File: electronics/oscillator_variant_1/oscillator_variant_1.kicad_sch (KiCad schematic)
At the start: 48 parts, among them J1 module_2x15_left_input, J2 module_2x15_right_input, J3 Coax, Q1 BC817, U1 TL081, U2 LME49720, U3 TL082, U4 TL431

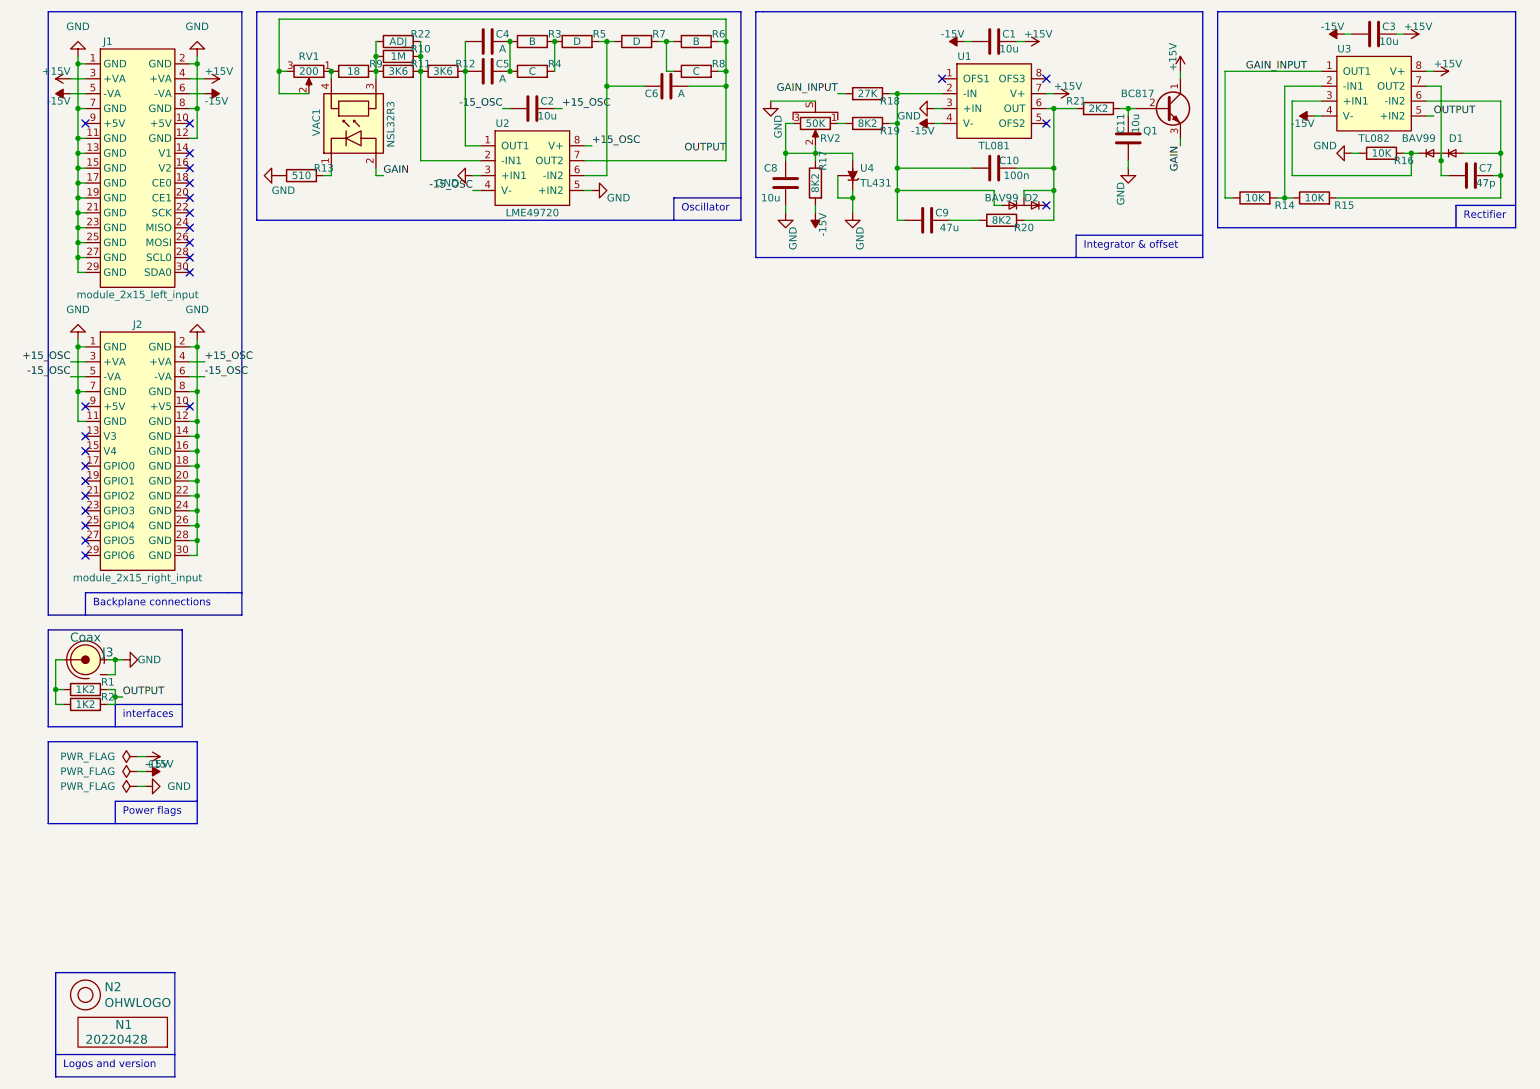
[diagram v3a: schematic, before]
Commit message: place and route and silk placement completed
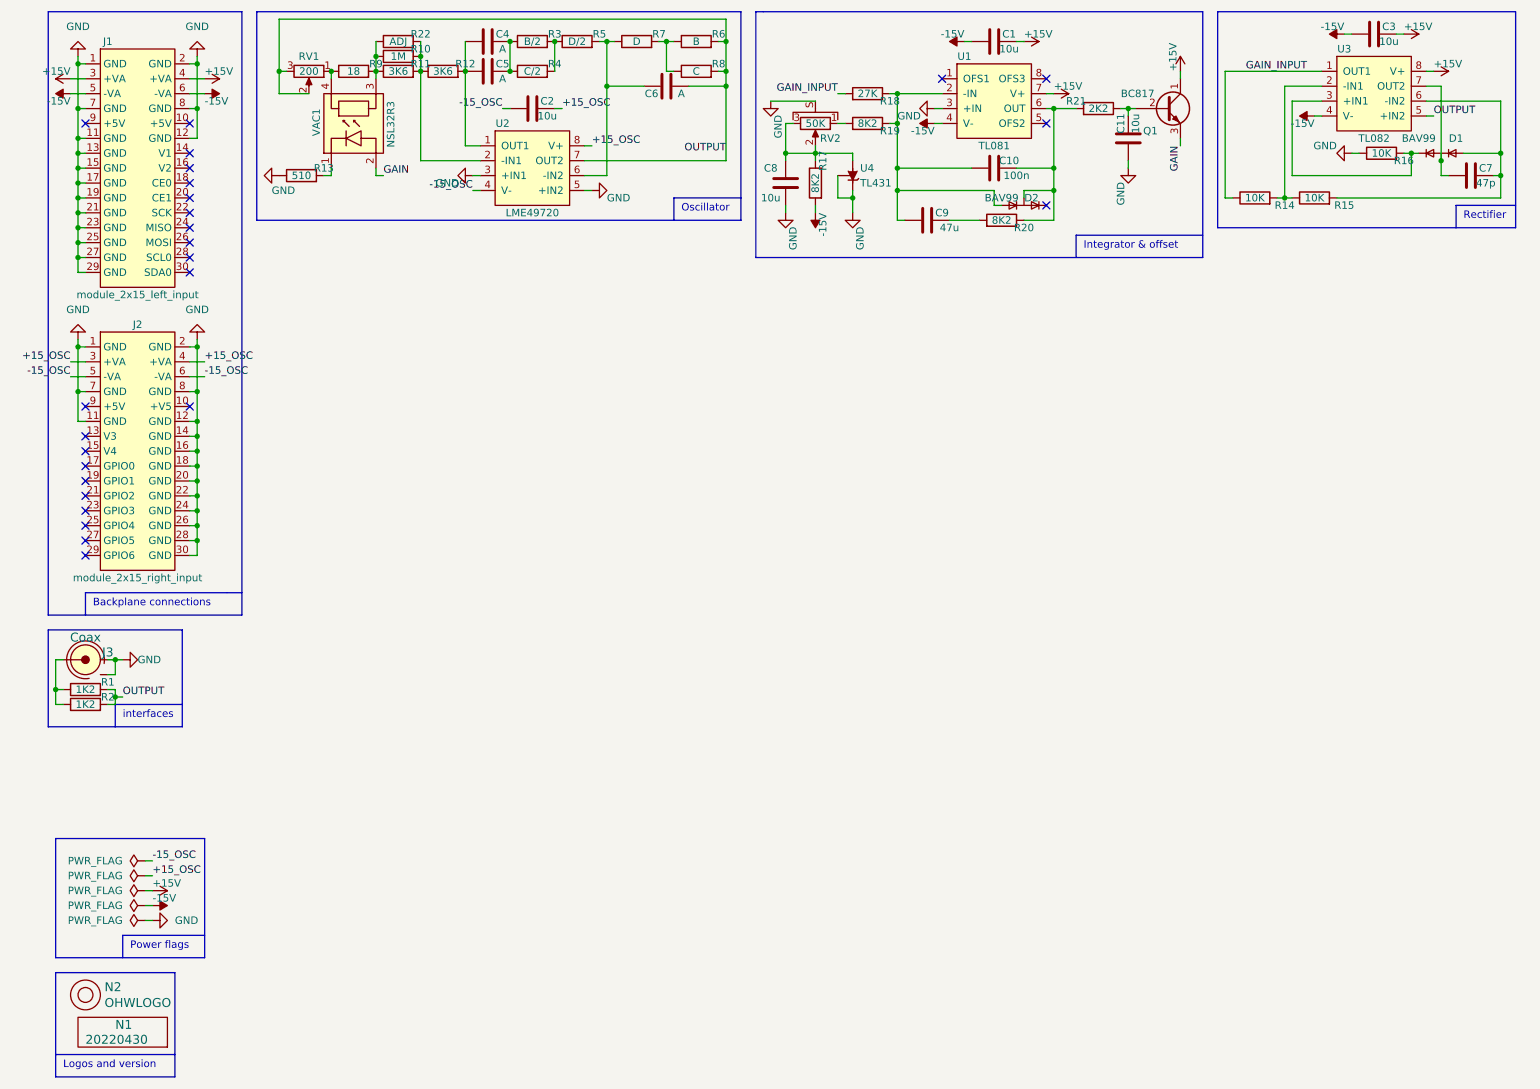
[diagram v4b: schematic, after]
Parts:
- J3: symbol SquantorConnectors:Coax_with_shield -> SquantorConnectors:Coax_shielded
- N1: value 20220428 -> 20220430
- R3: value B -> B/2
- R4: value C -> C/2
- R5: value D -> D/2

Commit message: small modification made to select output point
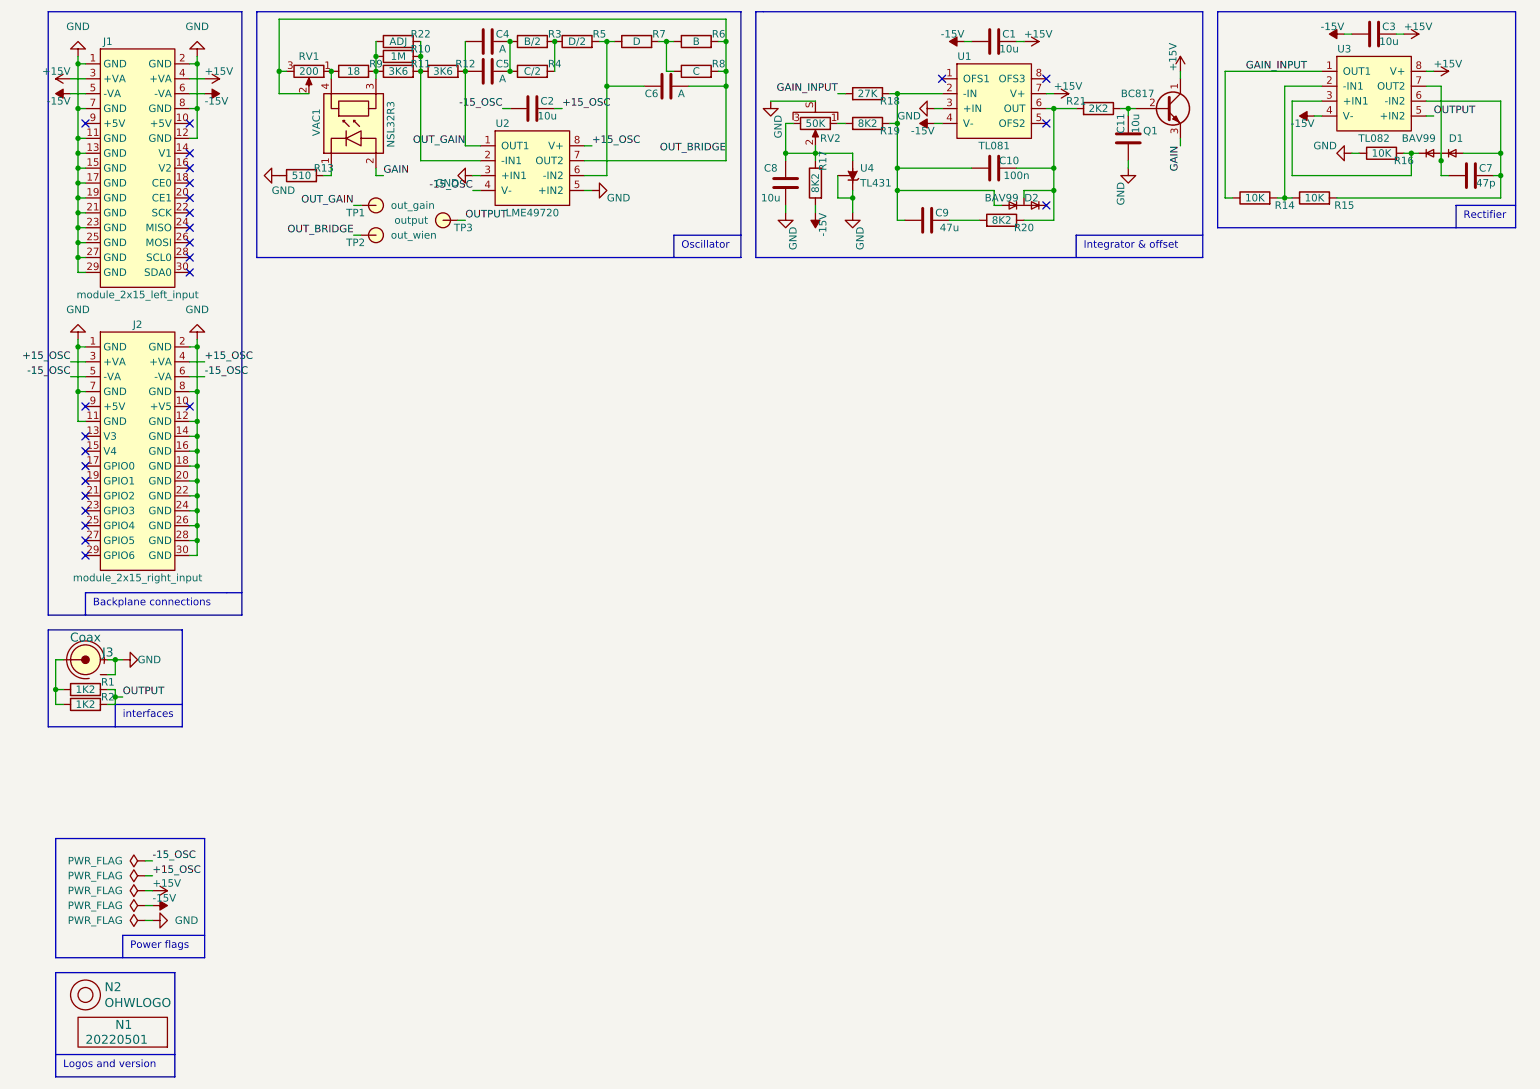
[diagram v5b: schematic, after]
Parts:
- added TP1: out_gain, SquantorTestPoints:TestPoint_hole_H04R07, symbol SquantorProto:testpad
- added TP2: out_wien, SquantorTestPoints:TestPoint_hole_H04R07, symbol SquantorProto:testpad
- added TP3: output, SquantorTestPoints:TestPoint_hole_H04R07, symbol SquantorProto:testpad
- N1: value 20220430 -> 20220501
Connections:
- net OUTPUT: now also TP3.1; no longer C6.2, R6.2, R8.2, RV1.2, RV1.3, U2.7 (OUT2)
- net OUT_GAIN: now reaches C4.1, C5.1, R12.2, U2.1 (OUT1)
- net OUT_GAIN: now also TP1.1
- new net OUT_BRIDGE: C6.2, R6.2, R8.2, RV1.2, RV1.3, TP2.1, U2.7 (OUT2)
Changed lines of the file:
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@@
     (stroke (width 0) (type default) (color 0 0 0 0))
   )
-  (polyline (pts (xy 132.08 49.53) (xy 132.08 13.97))
+  (polyline (pts (xy 132.08 55.88) (xy 132.08 13.97))
     (stroke (width 0) (type default) (color 0 0 0 0))
   )
@@
     (stroke (width 0) (type default) (color 0 0 0 0))
   )
+  (wire (pts (xy 83.82 49.53) (xy 85.09 49.53))
+    (stroke (width 0) (type default) (color 0 0 0 0))
+  )
   (wire (pts (xy 105.41 44.45) (xy 106.68 44.45))
     (stroke (width 0) (type default) (color 0 0 0 0))
@@
     (stroke (width 0) (type default) (color 0 0 0 0))
   )
-  (polyline (pts (xy 49.53 13.97) (xy 49.53 49.53))
+  (wire (pts (xy 66.04 52.07) (xy 67.31 52.07))
+    (stroke (width 0) (type default) (color 0 0 0 0))
+  )
+  (polyline (pts (xy 49.53 13.97) (xy 49.53 55.88))
     (stroke (width 0) (type default) (color 0 0 0 0))
   )
@@
     (stroke (width 0) (type default) (color 0 0 0 0))
   )
-  (polyline (pts (xy 120.65 45.72) (xy 120.65 49.53))
+  (polyline (pts (xy 120.65 52.07) (xy 120.65 55.88))
     (stroke (width 0) (type default) (color 0 0 0 0))
   )
@@
     (stroke (width 0) (type default) (color 0 0 0 0))
   )
+  (wire (pts (xy 66.04 46.99) (xy 67.31 46.99))
+    (stroke (width 0) (type default) (color 0 0 0 0))
+  )
   (wire (pts (xy 19.05 40.64) (xy 19.05 43.18))
     (stroke (width 0) (type default) (color 0 0 0 0))
@@
     (stroke (width 0) (type default) (color 0 0 0 0))
   )
-  (polyline (pts (xy 49.53 49.53) (xy 132.08 49.53))
+  (polyline (pts (xy 49.53 55.88) (xy 132.08 55.88))
     (stroke (width 0) (type default) (color 0 0 0 0))
   )
@@
     (stroke (width 0) (type default) (color 0 0 0 0))
   )
-  (polyline (pts (xy 132.08 45.72) (xy 120.65 45.72))
+  (polyline (pts (xy 132.08 52.07) (xy 120.65 52.07))
     (stroke (width 0) (type default) (color 0 0 0 0))
   )
@@
     (effects (font (size 1.27 1.27)) (justify left bottom))
   )
-  (text "Oscillator" (at 121.92 48.26 0)
+  (text "Oscillator" (at 121.92 54.61 0)
     (effects (font (size 1.27 1.27)) (justify left bottom))
   )
@@
     (effects (font (size 1.27 1.27)) (justify right bottom))
   )
+  (label "OUT_GAIN" (at 85.09 36.83 180)
+    (effects (font (size 1.27 1.27)) (justify right bottom))
+  )
   (label "-15_OSC" (at 17.78 76.2 180)
     (effects (font (size 1.27 1.27)) (justify right bottom))
   )
+  (label "OUT_BRIDGE" (at 66.04 52.07 180)
+    (effects (font (size 1.27 1.27)) (justify right bottom))
+  )
   (label "OUTPUT" (at 250.19 31.75 0)
     (effects (font (size 1.27 1.27)) (justify left bottom))
   )
-  (label "OUTPUT" (at 129.54 38.1 180)
+  (label "OUT_BRIDGE" (at 129.54 38.1 180)
     (effects (font (size 1.27 1.27)) (justify right bottom))
   )
@@
     (effects (font (size 1.27 1.27)) (justify right bottom))
   )
+  (label "OUT_GAIN" (at 66.04 46.99 180)
+    (effects (font (size 1.27 1.27)) (justify right bottom))
+  )
   (label "+15_OSC" (at 101.6 30.48 0)
     (effects (font (size 1.27 1.27)) (justify left bottom))
@@
     (effects (font (size 1.27 1.27)) (justify left bottom))
   )
+  (label "OUTPUT" (at 85.09 49.53 0)
+    (effects (font (size 1.27 1.27)) (justify left bottom))
+  )
   (symbol (lib_id "SquantorLabels:VYYYYMMDD") (at 26.67 189.23 0) (unit 1)
     (in_bom yes) (on_board yes)
@@
       (effects (font (size 1.524 1.524)) (justify left))
     )
-    (property "Value" "20220430" (id 1) (at 20.32 189.23 0)
+    (property "Value" "20220501" (id 1) (at 20.32 189.23 0)
       (effects (font (size 1.524 1.524)) (justify left))
     )
@@
     (pin "1")
     (pin "2")
+  )
+  (symbol (lib_id "SquantorProto:testpad") (at 81.28 49.53 180) (unit 1)
+    (in_bom yes) (on_board yes)
+    (property "Reference" "TP3" (id 0) (at 86.36 50.8 0)
+      (effects (font (size 1.27 1.27)) (justify left))
+    )
+    (property "Value" "output" (id 1) (at 78.74 49.53 0)
+      (effects (font (size 1.27 1.27)) (justify left))
+    )
+    (property "Footprint" "SquantorTestPoints:TestPoint_hole_H04R07" (id 2) (at 80.01 50.165 0)
+      (effects (font (size 1.27 1.27)) hide)
+    )
+    (property "Datasheet" "" (id 3) (at 80.01 50.165 0)
+      (effects (font (size 1.27 1.27)) hide)
+    )
+    (pin "1")
   )
   (symbol (lib_id "Device:R") (at 96.52 24.13 90) (unit 1)
@@
     (pin "2")
   )
+  (symbol (lib_id "SquantorProto:testpad") (at 69.85 52.07 0) (unit 1)
+    (in_bom yes) (on_board yes)
+    (property "Reference" "TP2" (id 0) (at 64.77 53.34 0)
+      (effects (font (size 1.27 1.27)) (justify left))
+    )
+    (property "Value" "out_wien" (id 1) (at 72.39 52.07 0)
+      (effects (font (size 1.27 1.27)) (justify left))
+    )
+    (property "Footprint" "SquantorTestPoints:TestPoint_hole_H04R07" (id 2) (at 71.12 51.435 0)
+      (effects (font (size 1.27 1.27)) hide)
+    )
+    (property "Datasheet" "" (id 3) (at 71.12 51.435 0)
+      (effects (font (size 1.27 1.27)) hide)
+    )
+    (pin "1")
+  )
   (symbol (lib_id "Device:R") (at 124.46 24.13 90) (unit 1)
     (in_bom yes) (on_board yes)
@@
     (pin "1")
     (pin "2")
+  )
+  (symbol (lib_id "SquantorProto:testpad") (at 69.85 46.99 0) (unit 1)
+    (in_bom yes) (on_board yes)
+    (property "Reference" "TP1" (id 0) (at 64.77 48.26 0)
+      (effects (font (size 1.27 1.27)) (justify left))
+    )
+    (property "Value" "out_gain" (id 1) (at 72.39 46.99 0)
+      (effects (font (size 1.27 1.27)) (justify left))
+    )
+    (property "Footprint" "SquantorTestPoints:TestPoint_hole_H04R07" (id 2) (at 71.12 46.355 0)
+      (effects (font (size 1.27 1.27)) hide)
+    )
+    (property "Datasheet" "" (id 3) (at 71.12 46.355 0)
+      (effects (font (size 1.27 1.27)) hide)
+    )
+    (pin "1")
   )
   (symbol (lib_id "Device:R") (at 20.32 129.54 90) (unit 1)
@@
     )
     (path "/00000000-0000-0000-0000-00005ee12bf3"
-      (reference "N1") (unit 1) (value "20220430") (footprint "SquantorLabels:Label_Generic")
+      (reference "N1") (unit 1) (value "20220501") (footprint "SquantorLabels:Label_Generic")
     )
     (path "/00000000-0000-0000-0000-00005ee13678"
@@
       (reference "RV2") (unit 1) (value "50K") (footprint "SquantorRcl:POT_ALPS_RK09K111")
     )
+    (path "/ce7614b3-9a8d-4fbe-9885-87e6bff9e768"
+      (reference "TP1") (unit 1) (value "out_gain") (footprint "SquantorTestPoints:TestPoint_hole_H04R07")
+    )
+    (path "/5a260b88-12aa-4187-8c39-a74fd63432d6"
+      (reference "TP2") (unit 1) (value "out_wien") (footprint "SquantorTestPoints:TestPoint_hole_H04R07")
+    )
+    (path "/36f4e3cc-a2b3-4b4f-8be6-db1d21e020b6"
+      (reference "TP3") (unit 1) (value "output") (footprint "SquantorTestPoints:TestPoint_hole_H04R07")
+    )
     (path "/eed9ea4c-7b8c-4ed4-b938-e17af65d7489"

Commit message: reviewed
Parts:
- N1: value 20220501 -> 20220507
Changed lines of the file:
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@@
       (effects (font (size 1.524 1.524)) (justify left))
     )
-    (property "Value" "20220501" (id 1) (at 20.32 189.23 0)
+    (property "Value" "20220507" (id 1) (at 20.32 189.23 0)
       (effects (font (size 1.524 1.524)) (justify left))
     )
@@
     )
     (path "/00000000-0000-0000-0000-00005ee12bf3"
-      (reference "N1") (unit 1) (value "20220501") (footprint "SquantorLabels:Label_Generic")
+      (reference "N1") (unit 1) (value "20220507") (footprint "SquantorLabels:Label_Generic")
     )
     (path "/00000000-0000-0000-0000-00005ee13678"

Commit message: fixed aisler warnings/errors
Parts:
- C4, C5, C6: footprint SquantorRcl:C-025_050-050X100-0805-3516-film -> SquantorRcl:C-050-050X100-0805-3516-film
- N1: value 20220507 -> 20220530
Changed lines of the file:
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@@
       (effects (font (size 1.524 1.524)) (justify left))
     )
-    (property "Value" "20220507" (id 1) (at 20.32 189.23 0)
+    (property "Value" "20220530" (id 1) (at 20.32 189.23 0)
       (effects (font (size 1.524 1.524)) (justify left))
     )
@@
     (property "Reference" "C6" (id 0) (at 116.84 27.94 90))
     (property "Value" "A" (id 1) (at 121.92 27.94 90))
-    (property "Footprint" "SquantorRcl:C-025_050-050X100-0805-3516-film" (id 2) (at 123.19 25.7048 0)
+    (property "Footprint" "SquantorRcl:C-050-050X100-0805-3516-film" (id 2) (at 123.19 25.7048 0)
       (effects (font (size 1.27 1.27)) hide)
     )
@@
     (property "Reference" "C5" (id 0) (at 91.44 22.86 90))
     (property "Value" "A" (id 1) (at 91.44 25.4 90))
-    (property "Footprint" "SquantorRcl:C-025_050-050X100-0805-3516-film" (id 2) (at 92.71 23.1648 0)
+    (property "Footprint" "SquantorRcl:C-050-050X100-0805-3516-film" (id 2) (at 92.71 23.1648 0)
       (effects (font (size 1.27 1.27)) hide)
     )
@@
     (property "Reference" "C4" (id 0) (at 91.44 17.78 90))
     (property "Value" "A" (id 1) (at 91.44 20.32 90))
-    (property "Footprint" "SquantorRcl:C-025_050-050X100-0805-3516-film" (id 2) (at 92.71 18.0848 0)
+    (property "Footprint" "SquantorRcl:C-050-050X100-0805-3516-film" (id 2) (at 92.71 18.0848 0)
       (effects (font (size 1.27 1.27)) hide)
     )
@@
     )
     (path "/b51ccab4-4241-4333-b251-d201fcd5e558"
-      (reference "C4") (unit 1) (value "A") (footprint "SquantorRcl:C-025_050-050X100-0805-3516-film")
+      (reference "C4") (unit 1) (value "A") (footprint "SquantorRcl:C-050-050X100-0805-3516-film")
     )
     (path "/2f8578f6-29b3-46c0-be78-3b257f29f7dd"
-      (reference "C5") (unit 1) (value "A") (footprint "SquantorRcl:C-025_050-050X100-0805-3516-film")
+      (reference "C5") (unit 1) (value "A") (footprint "SquantorRcl:C-050-050X100-0805-3516-film")
     )
     (path "/1a6a52f9-6b08-4411-9f3c-a37445b04753"
-      (reference "C6") (unit 1) (value "A") (footprint "SquantorRcl:C-025_050-050X100-0805-3516-film")
+      (reference "C6") (unit 1) (value "A") (footprint "SquantorRcl:C-050-050X100-0805-3516-film")
     )
     (path "/b63a5da9-8066-4614-a4b4-b99c80f29aec"
@@
     )
     (path "/00000000-0000-0000-0000-00005ee12bf3"
-      (reference "N1") (unit 1) (value "20220507") (footprint "SquantorLabels:Label_Generic")
+      (reference "N1") (unit 1) (value "20220530") (footprint "SquantorLabels:Label_Generic")
     )
     (path "/00000000-0000-0000-0000-00005ee13678"
